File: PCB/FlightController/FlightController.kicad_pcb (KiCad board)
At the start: 4 copper layers, 36 x 36 mm, 55 parts, among them J1 SM04B-GHS-TB_LF__SN_-, J2 SM03B-GHS-TB_LF__SN_, J3 USB-C, J4 SM06B-GHS-TB_LF__SN_, J5 SD_CARD_SLOT, SW1 TactileSwitch, SW2 TactileSwitch, U1 STM32F411CEU6, U2 ICM-42688-P, U3 BMP581, U4 CP2102N-A02-GQFN28R, U5 3.3Converter

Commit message: Update PCB Layout
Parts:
- removed C1: 4u7, Capacitor_SMD:C_0402_1005Metric
- removed C2: 0u1, Capacitor_SMD:C_0402_1005Metric
- removed D3, D4: LED, LED_SMD:LED_0603_1608Metric
- removed D5: SP0503BAHT, Package_TO_SOT_SMD:SOT-143
- removed J3: USB-C, FlightControllerFootprints:GCT_USB4050-XX-X_REVA
- removed R5: 47k5, Resistor_SMD:R_0402_1005Metric
- removed R6: 22k1, Resistor_SMD:R_0402_1005Metric
- removed R7: 1k, Resistor_SMD:R_0402_1005Metric
- removed R8, R9: 220, Resistor_SMD:R_0402_1005Metric
- removed SW2: TactileSwitch, FlightControllerFootprints:TE_FSM4JSMA
- added J7: TYPE-C-31-M-12, FlightControllerFootprints:HRO_TYPE-C-31-M-12, F.Cu at (152.5, 87.5)
- added SW3: SW_Push, Button_Switch_SMD:SW_SPST_PTS810, F.Cu at (129.1, 102.6)
- added U6: USBLC6-2SC6, Package_TO_SOT_SMD:SOT-23-6, F.Cu at (142.4, 85.3)
- C11, J1, J4, J5, R14, R16, R2: moved to B.Cu
- C3: footprint Capacitor_SMD:C_0402_1005Metric -> Capacitor_SMD:C_0603_1608Metric
- R3, R4: value 5k1 -> 5K1; moved to B.Cu
- SW1: value TactileSwitch -> SW_Push; footprint FlightControllerFootprints:TE_FSM4JSMA -> Button_Switch_SMD:SW_SPST_PTS810
- U4: value CP2102N-A02-GQFN28R -> ~; footprint FlightControllerFootprints:IC_CP2102N-A02-GQFN28R -> FlightControllerFootprints:Solder Pad
- moved J5 49.3 mm to (136.0, 102.7)
- moved D7 40.5 mm to (137.0, 78.7), turned to -90 degrees
- moved C4 40.2 mm to (127.1, 79.1)
- moved C5 39.1 mm to (140.9, 93.2), turned to 180 degrees
- moved C10 38.7 mm to (140.4, 90.0), turned to -90 degrees
- moved J2 36.8 mm to (145.0, 77.9), turned to 180 degrees
- moved U1 36.7 mm to (134.5, 86.0)
- moved C9 36.5 mm to (139.2, 90.0), turned to -90 degrees
- moved R4 36.1 mm to (145.5, 85.8), turned to 180 degrees
- moved R15 33.5 mm to (134.6, 79.3), turned to 180 degrees
- moved U3 33.5 mm to (126.3, 80.9)
- moved R3 32.0 mm to (145.4, 89.0), turned to 180 degrees
- moved R1 31.8 mm to (132.1, 77.8)
- moved R12 31.8 mm to (124.7, 84.7)
- moved C6 31.7 mm to (140.9, 94.3)
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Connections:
- C3 pad 1: Net-(D1-A) -> Net-(D1-K)
- D1 pad 1: /VESC -> Net-(D1-K)
- D1 pad 2: Net-(D1-A) -> /VESC
- D2 pad 1: /VBUS -> Net-(D1-K)
- D2 pad 2: Net-(D1-A) -> VBUS
- J1 pad SH1: SHIELD_1 -> SHIELD
- J1 pad SH2: SHIELD -> SHIELD_1
- J2 pad 1: /VBUS -> VBUS
- R3 pad 1: GND -> Net-(J7-CC1)
- R3 pad 2: Net-(J3-CC1) -> GND
- SW1 pad 1: GND -> /BOOT0
- SW1 pad 2: GND -> VDD
- U1 pad 32: /GPS_RX -> /STM_D-
- U1 pad 33: /GPS_TX -> /STM_D+
- U1 pad 42: /CP_RX -> /GPS_TX
- U1 pad 43: /CP_TX -> /GPS_RX
- U4 pad 1: unconnected-(U4-DCD-Pad1) -> /VBAT
- U5 pad 1: Net-(D1-A) -> Net-(D1-K)
- U5 pad 3: Net-(D1-A) -> Net-(D1-K)
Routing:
- net GND: track 0.00 -> 45.1 mm, vias 0 -> 29
- net /M4: track 0.00 -> 29.2 mm, vias 0 -> 2
- net VBUS: track 0.00 -> 27.4 mm
- net VDD: track 0.00 -> 27.1 mm, vias 0 -> 17
- net /M3: track 0.00 -> 23.1 mm, vias 0 -> 4
- net /M2: track 0.00 -> 22.4 mm, vias 0 -> 2
- net Net-(D1-K): track 0.00 -> 20.7 mm
- net /M1: track 0.00 -> 18.1 mm, vias 0 -> 2
- net Net-(U1-PA0-WKUP): track 0.00 -> 9.05 mm
- net /VESC: track 0.00 -> 8.17 mm
- net /D+: track 0.00 -> 5.28 mm
- net /D-: track 0.00 -> 4.62 mm
- net /STM_D-: track 0.00 -> 3.78 mm
- net /STM_D+: track 0.00 -> 3.49 mm
- net /VBAT: track 0.00 -> 3.11 mm
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- added copper zone on F.Cu, net GND
- added copper zone on In1.Cu, net GND
- added copper zone on F.Cu, net VDD
- added copper zone on In2.Cu, net VDD

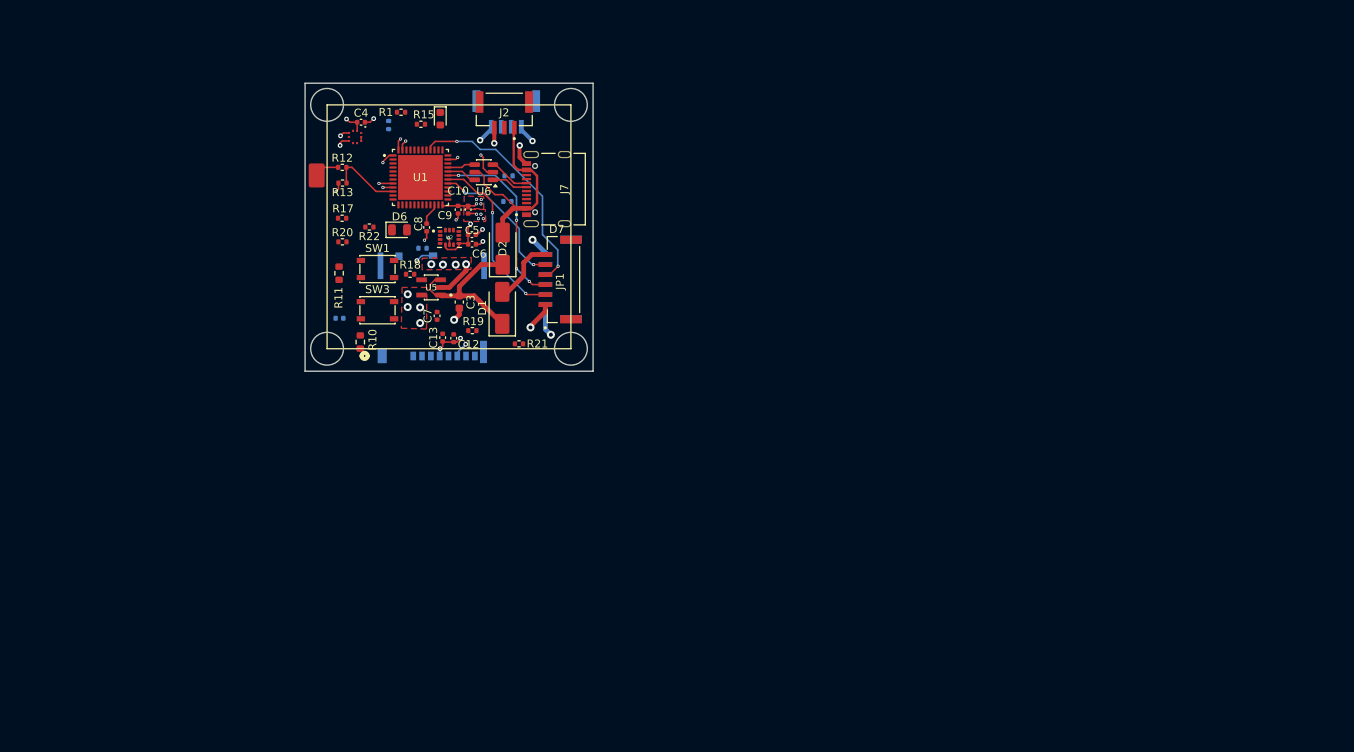
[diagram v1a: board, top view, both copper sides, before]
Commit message: Addition of Onboard Buck: Schematic and Layout Update
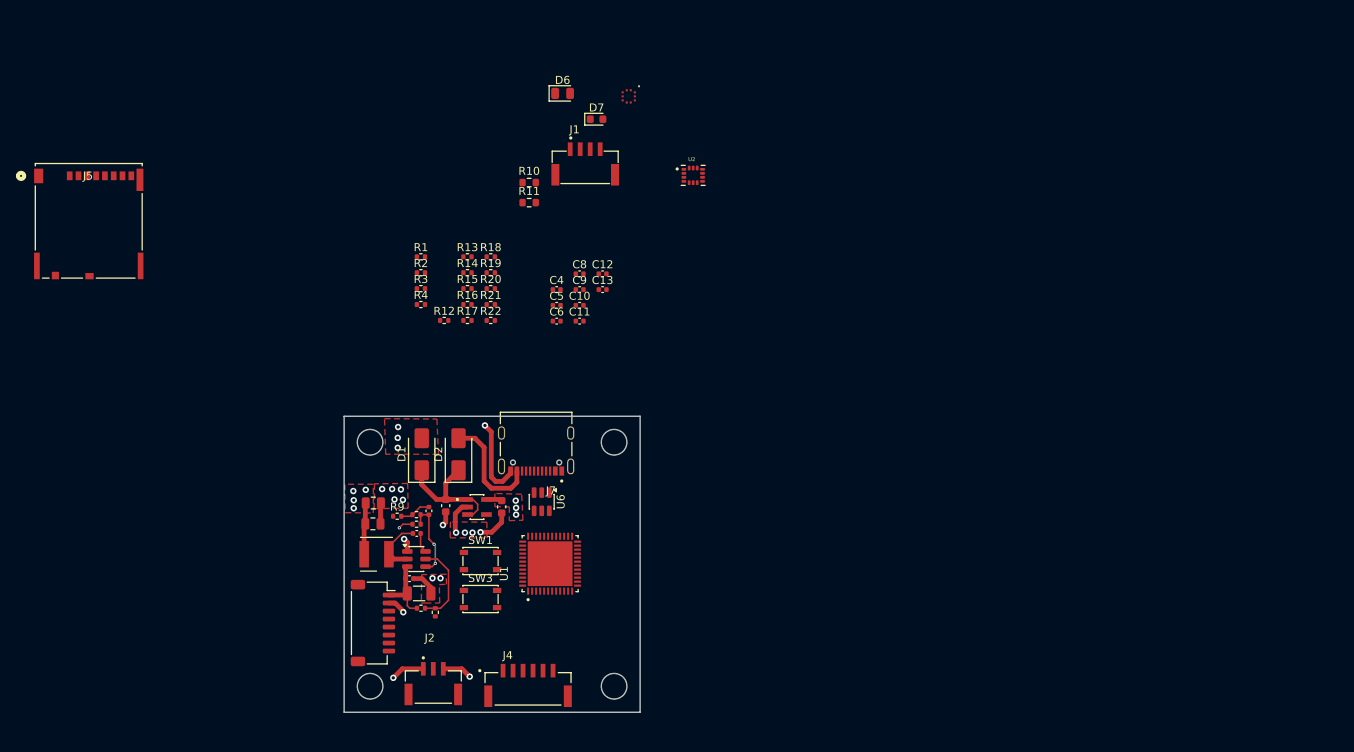
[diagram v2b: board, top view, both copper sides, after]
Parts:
- removed JP1: SM06B-SRSS-TB, FlightControllerFootprints:JST_SM06B-GHS-TB_LF__SN_
- removed U4: ~, FlightControllerFootprints:Solder Pad
- added C1: 0u1, Capacitor_SMD:C_0402_1005Metric, F.Cu at (133.1, 136.2)
- added C14: 75p, Capacitor_SMD:C_0402_1005Metric, F.Cu at (135.6, 127.7)
- added C15: 0u1, Capacitor_SMD:C_0402_1005Metric, F.Cu at (134.0, 130.5)
- added C16: 22u, Capacitor_SMD:C_0805_2012Metric, F.Cu at (128.6, 129.3)
- added C17: 22u, Capacitor_SMD:C_0805_2012Metric, F.Cu at (128.6, 126.7)
- added C2: 10u, Capacitor_SMD:C_1206_3216Metric, F.Cu at (134.3, 138.0)
- added L1: 10u, Inductor_SMD_Wurth:L_Wurth_WE-LQSH-4020, F.Cu at (129.0, 133.1)
- added R5: 105k, Resistor_SMD:R_0402_1005Metric, F.Cu at (136.3, 140.4)
- added R6: 13k, Resistor_SMD:R_0402_1005Metric, F.Cu at (134.0, 129.3)
- added R7: 100k, Resistor_SMD:R_0402_1005Metric, F.Cu at (134.0, 128.2)
- added R8: 511k, Resistor_SMD:R_0402_1005Metric, F.Cu at (134.6, 139.8)
- added R9: 50, Resistor_SMD:R_0402_1005Metric, F.Cu at (131.6, 128.3)
- added U7: TPS54302, Package_TO_SOT_SMD:SOT-23-6, F.Cu at (134.0, 133.7)
- added U8: ~, Connector_JST:JST_SH_SM08B-SRSS-TB_1x08-1MP_P1.00mm_Horizontal, F.Cu at (128.6, 141.7)
- C11, J1, J4, J5, R14, R16, R2, R3, R4: moved to F.Cu
- C7: footprint Capacitor_SMD:C_0402_1005Metric -> Capacitor_SMD:C_0603_1608Metric
- moved J2 71.9 mm to (136.1, 149.3), turned to 0 degrees
- moved J4 50.9 mm to (147.9, 149.5), turned to 0 degrees
- moved U1 50.9 mm to (150.7, 134.3), turned to 90 degrees
- moved J5 44.4 mm to (93.0, 91.4)
- moved U6 41.8 mm to (149.7, 126.5), turned to -90 degrees
- moved SW1 38.7 mm to (142.0, 133.9)
- moved SW3 38.3 mm to (142.0, 138.7)
- moved U3 34.6 mm to (160.5, 75.9)
- moved C4 32.2 mm to (151.5, 100.0)
- moved U2 31.4 mm to (168.6, 85.7)
- moved J7 30.7 mm to (148.9, 118.0), turned to 180 degrees
- moved C11 30.0 mm to (154.4, 104.0), turned to 0 degrees
- moved R10 29.0 mm to (148.1, 86.6), turned to 0 degrees
- moved U5 28.0 mm to (141.6, 127.2), turned to 0 degrees
- moved D6 26.6 mm to (152.3, 75.5)
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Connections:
- D1 pad 2: /VESC -> /5V
- J1 pad SH1: SHIELD -> SHIELD_1
- J1 pad SH2: SHIELD_1 -> SHIELD
- J2 pad 1: VBUS -> /5V
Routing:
- net /M4: track 29.2 -> 0.00 mm, vias 2 -> 0
- net VDD: track 27.1 -> 1.97 mm, vias 17 -> 3
- net /M3: track 23.1 -> 0.00 mm, vias 4 -> 0
- net /M2: track 22.4 -> 0.00 mm, vias 2 -> 0
- net /M1: track 18.1 -> 0.00 mm, vias 2 -> 0
- net VBUS: track 27.4 -> 14.1 mm
- net /5V: track 0.00 -> 10.7 mm, vias 0 -> 8
- net Net-(U7-EN): track 0.00 -> 10.5 mm
- net Net-(U7-FB): track 0.00 -> 10.1 mm, vias 0 -> 2
- net Net-(U1-PA0-WKUP): track 9.05 -> 0.00 mm
- net GND: track 45.1 -> 36.1 mm, vias 29 -> 17
- net /VESC: track 8.17 -> 0.00 mm
- net Net-(U7-SW): track 0.00 -> 7.21 mm
- net /VBAT: track 3.11 -> 8.77 mm
- net /D+: track 5.28 -> 0.00 mm
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- added copper zone on F.Cu, net /5V
- added copper zone on In2.Cu, net /5V
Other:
- board size 36 x 36 mm -> 37 x 37 mm

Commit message: Update Layout
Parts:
- removed J4: SM06B-GHS-TB_LF__SN_, FlightControllerFootprints:JST_SM06B-GHS-TB_LF__SN_
- added C18: 10p, Capacitor_SMD:C_0402_1005Metric, F.Cu at (145.9, 142.1)
- added C19: 10p, Capacitor_SMD:C_0402_1005Metric, F.Cu at (154.2, 142.1)
- added J3: SM04B-GHS-TB_LF__SN_-, FlightControllerFootprints:JST_SM04B-GHS-TB_LF__SN_-, F.Cu at (135.8, 150.2)
- added Y1: Crystal, Crystal:Crystal_SMD_5032-2Pin_5.0x3.2mm, F.Cu at (149.9, 141.6)
- J2: value SM03B-GHS-TB_LF__SN_ -> SM04B-GHS-TB_LF__SN_-; footprint FlightControllerFootprints:JST_SM03B-GHS-TB_LF__SN_ -> FlightControllerFootprints:JST_SM04B-GHS-TB_LF__SN_-; moved to B.Cu
- J5: moved to B.Cu
- moved D7 82.0 mm to (126.5, 155.1)
- moved D6 82.0 mm to (122.2, 151.8)
- moved J5 72.0 mm to (154.5, 128.9), turned to 90 degrees
- moved U3 70.8 mm to (155.4, 146.5)
- moved J1 65.8 mm to (148.0, 150.2)
- moved U2 54.2 mm to (158.3, 139.0)
- moved R16 45.5 mm to (158.1, 143.8)
- moved R18 41.0 mm to (159.7, 133.5), turned to 180 degrees
- moved C5 40.5 mm to (160.6, 141.5), turned to 90 degrees
- moved C6 37.8 mm to (159.0, 141.0), turned to 180 degrees
- moved R17 35.7 mm to (157.5, 135.2)
- moved R22 32.8 mm to (157.5, 133.4)
- moved C9 31.0 mm to (155.4, 131.0), turned to 90 degrees
- moved C12 30.5 mm to (157.0, 128.6), turned to -90 degrees
- moved C10 29.1 mm to (156.6, 131.0), turned to 90 degrees
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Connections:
- J1 pad SH1: SHIELD_1 -> SHIELD
- J2 pad 1: /5V -> VDD
- J2 pad 2: /ELRS -> /SDA
- J2 pad 3: GND -> /SCL
- R12 pad 2: Net-(U1-PA0-WKUP) -> /V_ADC
- R13 pad 1: Net-(U1-PA0-WKUP) -> /V_ADC
- U1 pad 10: Net-(U1-PA0-WKUP) -> /M4
- U1 pad 11: unconnected-(U1-PA1-Pad11) -> /M3
- U1 pad 12: /ELRS -> /M2
- U1 pad 13: unconnected-(U1-PA3-Pad13) -> /M1
- U1 pad 19: unconnected-(U1-PB1-Pad19) -> /V_ADC
- U1 pad 29: /M1 -> unconnected-(U1-PA8-Pad29)
- U1 pad 30: /M2 -> unconnected-(U1-PA9-Pad30)
- U1 pad 31: /M3 -> unconnected-(U1-PA10-Pad31)
- U1 pad 40: /M4 -> unconnected-(U1-PB4-Pad40)
- U1 pad 42: /GPS_TX -> /ELRS_RX
- U1 pad 43: /GPS_RX -> /ELRS_TX
- U1 pad 5: unconnected-(U1-PH0-OSC_IN-Pad5) -> Net-(U1-PH0-OSC_IN)
- U1 pad 6: unconnected-(U1-PH1-OSC_OUT-Pad6) -> Net-(U1-PH1-OSC_OUT)
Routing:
- net /M1: track 0.00 -> 32.7 mm, vias 0 -> 2
- net /M2: track 0.00 -> 30.9 mm, vias 0 -> 2
- net VDD: track 1.97 -> 31.9 mm, vias 3 -> 18
- net GND: track 36.1 -> 62.0 mm, vias 17 -> 40
- net /M3: track 0.00 -> 25.2 mm, vias 0 -> 2
- net /M4: track 0.00 -> 24.1 mm, vias 0 -> 2
- net /IMU_CS: track 0.00 -> 17.7 mm, vias 0 -> 2
- net /DET: track 0.00 -> 16.1 mm, vias 0 -> 1
- net /SD_MISO: track 0.00 -> 15.3 mm, vias 0 -> 2
- net /SD_MOSI: track 0.00 -> 14.3 mm, vias 0 -> 2
- net /SD_CS: track 0.00 -> 13.3 mm, vias 0 -> 2
- net VBUS: track 14.1 -> 27.2 mm, vias 0 -> 2
- net Net-(J7-CC2): track 0.00 -> 10.2 mm
- net /SD_SCK: track 0.00 -> 9.63 mm, vias 0 -> 1
- net Net-(U1-PH0-OSC_IN): track 0.00 -> 6.94 mm
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
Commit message: Update Schematic
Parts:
- R10: footprint Resistor_SMD:R_0603_1608Metric -> Resistor_SMD:R_0402_1005Metric
- R11: footprint Resistor_SMD:R_0603_1608Metric -> Resistor_SMD:R_0402_1005Metric; moved to B.Cu
- R14, R15: moved to B.Cu
- moved R10 54.1 mm to (141.6, 140.3), turned to 90 degrees
- moved R2 53.0 mm to (145.1, 149.9), turned to 90 degrees
- moved R14 51.3 mm to (159.6, 145.5), turned to 180 degrees
- moved R1 50.5 mm to (141.6, 145.9)
- moved C4 50.0 mm to (143.1, 149.3), turned to 180 degrees
- moved R11 43.6 mm to (144.4, 132.6), turned to -90 degrees
- moved C11 38.2 mm to (142.7, 140.4), turned to -90 degrees
- moved R12 37.6 mm to (134.4, 141.3)
- moved D6 35.7 mm to (157.5, 146.0)
- moved C8 34.3 mm to (156.7, 132.2)
- moved R15 30.6 mm to (145.3, 130.1), turned to -90 degrees
- moved D7 30.5 mm to (144.3, 130.2)
- moved U3 12.4 mm to (143.1, 147.6), turned to -90 degrees
- moved R13 11.1 mm to (142.8, 106.8)
- moved J1 2.51 mm to (150.5, 149.7)
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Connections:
- J3 pad 2: /ELRS_TX -> /ELRS_RX
- J3 pad 3: /ELRS_RX -> /ELRS_TX
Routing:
- net /SCL: track 0.00 -> 31.7 mm, vias 0 -> 4
- net GND: track 62.0 -> 92.5 mm, vias 40 -> 44
- net /SWDCLK: track 0.00 -> 28.6 mm, vias 0 -> 2
- net /SWDIO: track 0.00 -> 24.3 mm, vias 0 -> 4
- net /SDA: track 0.00 -> 23.8 mm, vias 0 -> 2
- net VDD: track 31.9 -> 54.7 mm, vias 18 -> 27
- net /ELRS_RX: track 0.00 -> 20.6 mm, vias 0 -> 2
- net /ELRS_TX: track 0.00 -> 19.3 mm, vias 0 -> 2
- net /NRST: track 0.00 -> 16.4 mm, vias 0 -> 2
- net /BOOT0: track 0.00 -> 12.1 mm, vias 0 -> 1
- net Net-(U1-PB5): track 0.00 -> 6.07 mm, vias 0 -> 1
- net Net-(D6-A): track 0.00 -> 4.06 mm, vias 0 -> 1
- net Net-(D7-A): track 0.00 -> 2.76 mm, vias 0 -> 1
- net Net-(U1-VCAP_1): track 0.00 -> 2.35 mm
- net /M3: track 25.2 -> 26.9 mm
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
